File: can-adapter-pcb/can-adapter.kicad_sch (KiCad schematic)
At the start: 0 parts

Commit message: can-adapter-pcb: Add PIC18 microcontroller to schematic with ICSP programming header
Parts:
- added IC1: PIC18F26Q83T-I_5N, QFN65P600X600X100-29N-D, symbol PIC18F26Q83T-I5N:PIC18F26Q83T-I_5N
- added J1: ICSP, symbol Connector:Conn_01x06_Socket
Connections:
- new net +5V: IC1.17 (VDD), J1.2 (Pin_2)
- new net GND: IC1.16 (VSS_2), IC1.29 (EP), IC1.5 (VSS_1), J1.3 (Pin_3)
- new net ICSPCLK: IC1.25 (RB7/ICSPDAT), J1.5 (Pin_5)
- new net ICSPDAT: IC1.24 (RB6/ICSPCLK), J1.4 (Pin_4)
- new net VPP: IC1.26 (RE3/~{MCLR}/VPP), J1.1 (Pin_1)
- no-connect marks 0 -> 1

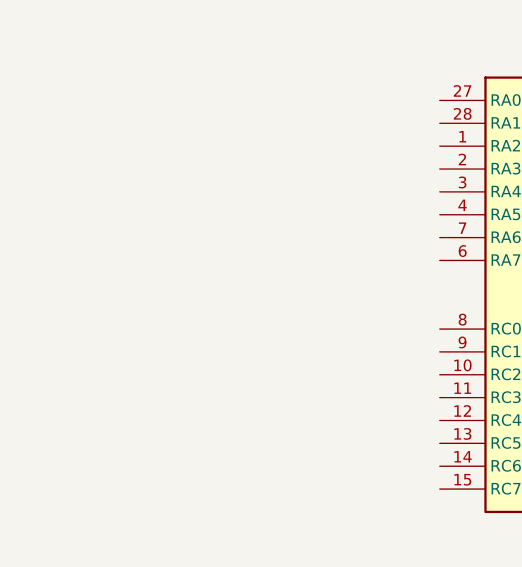
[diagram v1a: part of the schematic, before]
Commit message: can-adapter-pcb: Add tank and decoupling capacitor
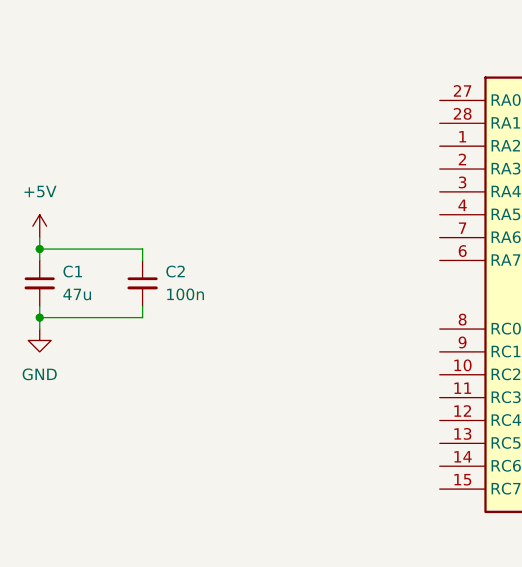
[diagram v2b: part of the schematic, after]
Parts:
- added C1: 47u, symbol Device:C_Small
- added C2: 100n, symbol Device:C_Small
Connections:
- net +5V: now also C1.1, C2.1
- net GND: now also C1.2, C2.2

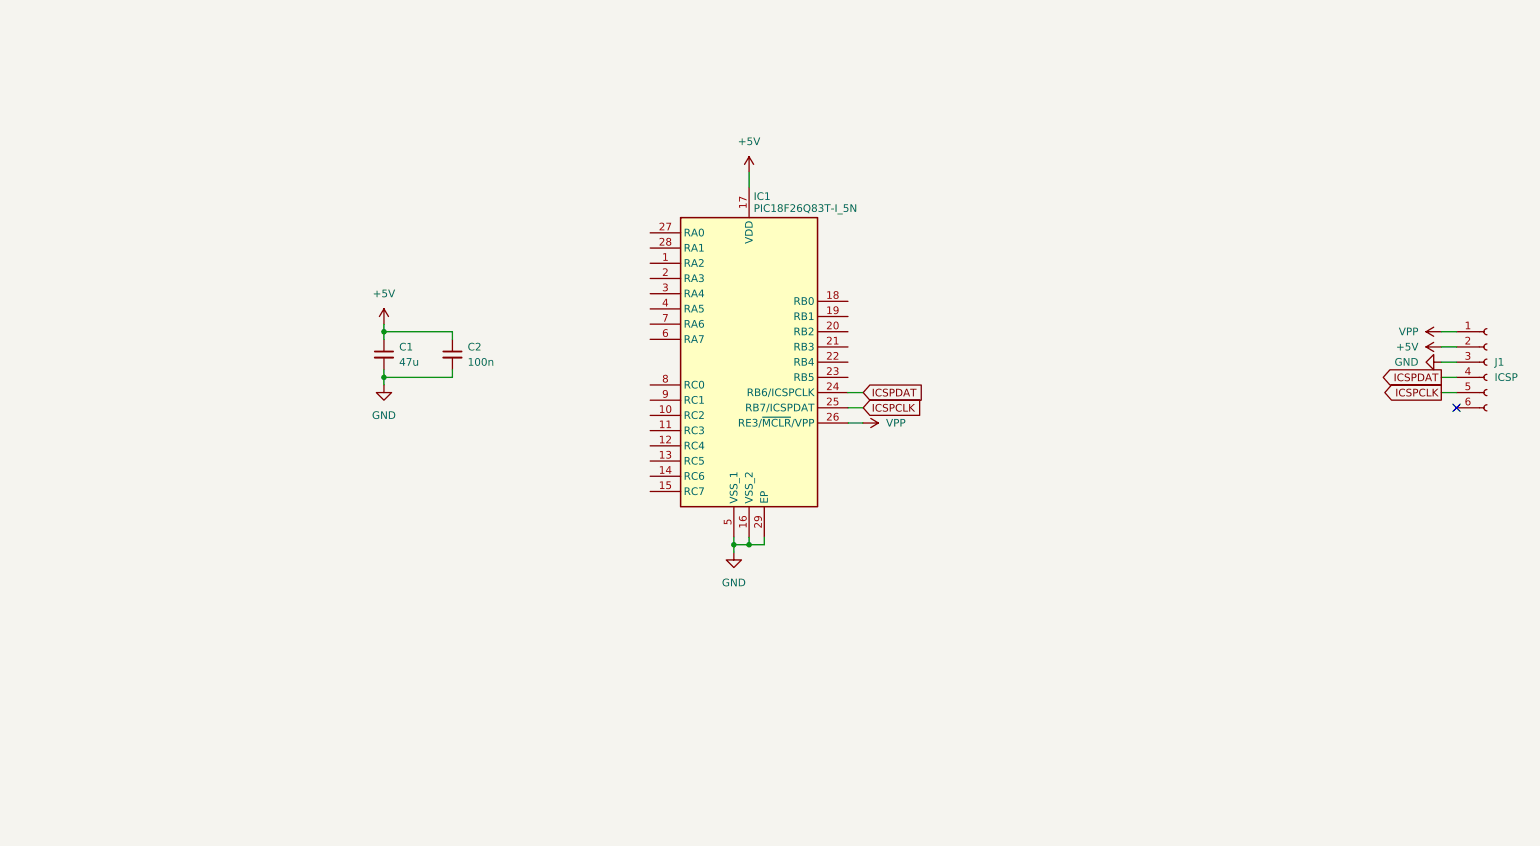
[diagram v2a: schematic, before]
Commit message: can-adapter-pcb: Add CAN transceiver to schematic
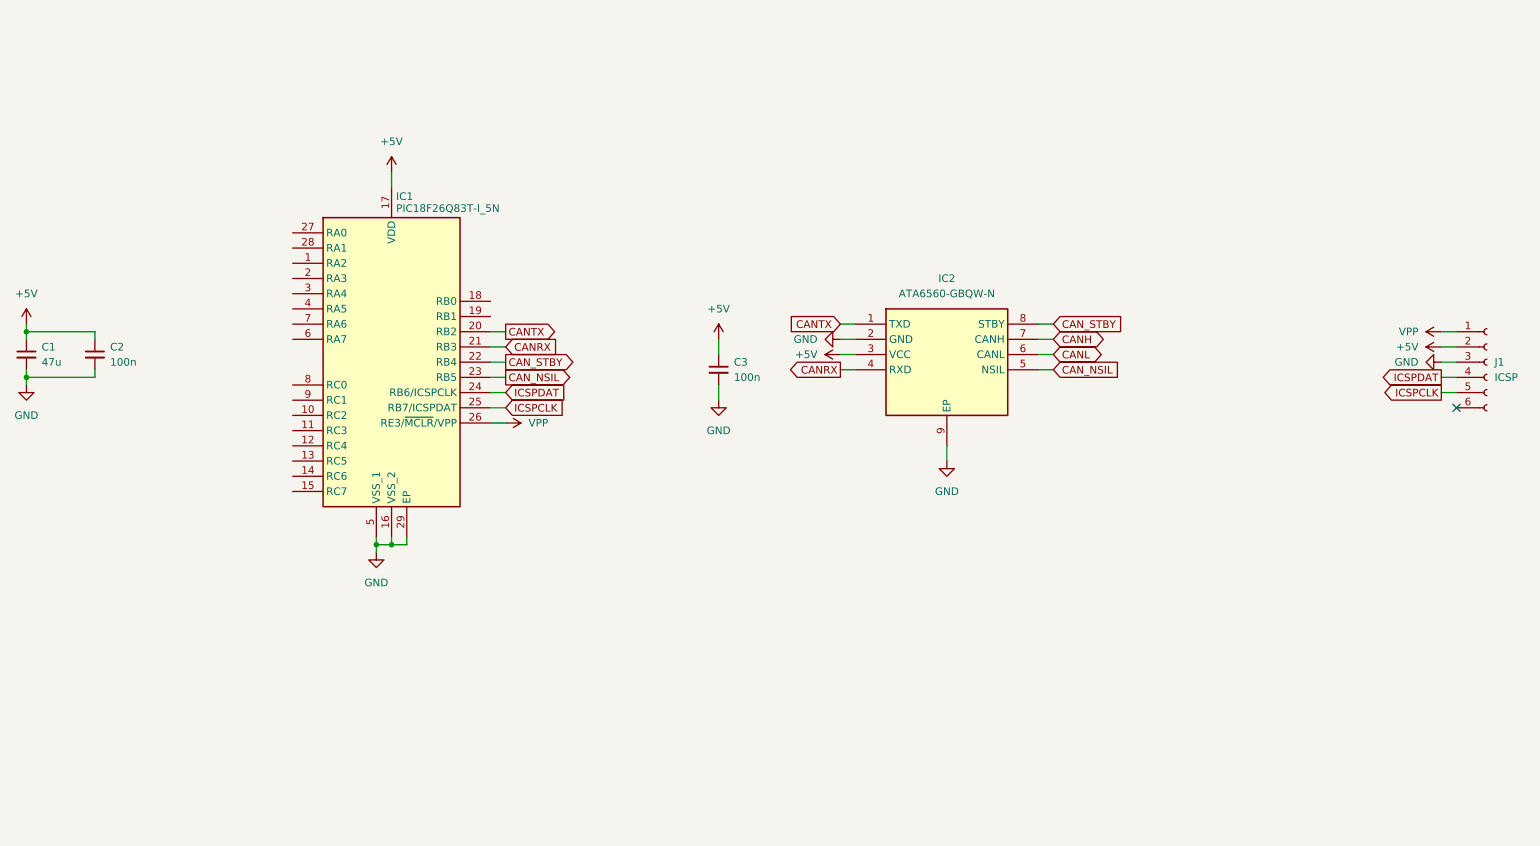
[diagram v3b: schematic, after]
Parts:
- added C3: 100n, symbol Device:C_Small
- added IC2: ATA6560-GBQW-N, SON65P300X300X90-9N-D, symbol ATA6560-GBQW-N:ATA6560-GBQW-N
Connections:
- net +5V: now also C3.1, IC2.3 (VCC)
- net GND: now also C3.2, IC2.2 (GND), IC2.9 (EP)
- net CANTX: now reaches IC1.20 (RB2)
- net CANTX: now also IC2.1 (TXD)
- net CANRX: now reaches IC1.21 (RB3)
- net CANRX: now also IC2.4 (RXD)
- net CAN_STBY: now reaches IC1.22 (RB4)
- net CAN_STBY: now also IC2.8 (STBY)
- net CAN_NSIL: now reaches IC1.23 (RB5)
- net CAN_NSIL: now also IC2.5 (NSIL)
- new net CANH: IC2.7 (CANH)
- new net CANL: IC2.6 (CANL)
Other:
- moved on the sheet: C1, C2, IC1

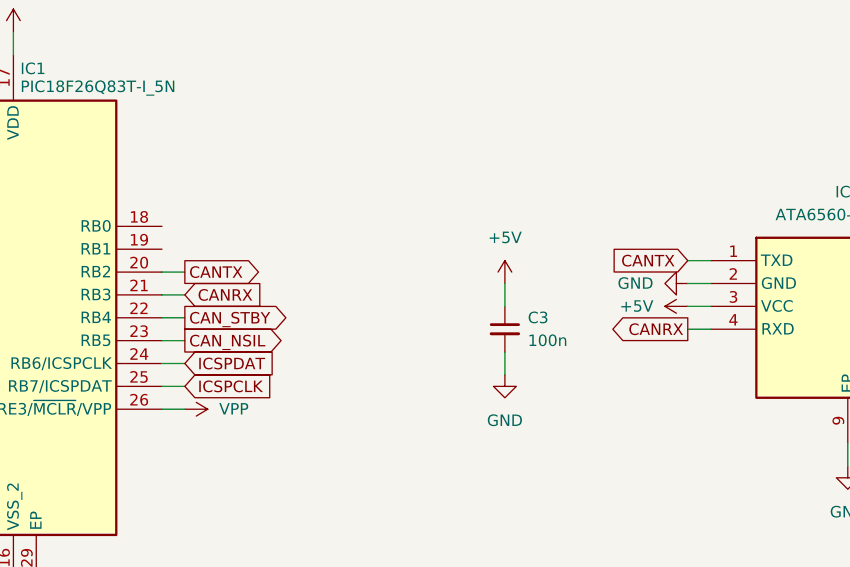
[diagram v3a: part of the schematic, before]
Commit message: can-adapter-pcb: Swap pins around, add UART debug pins on MCU
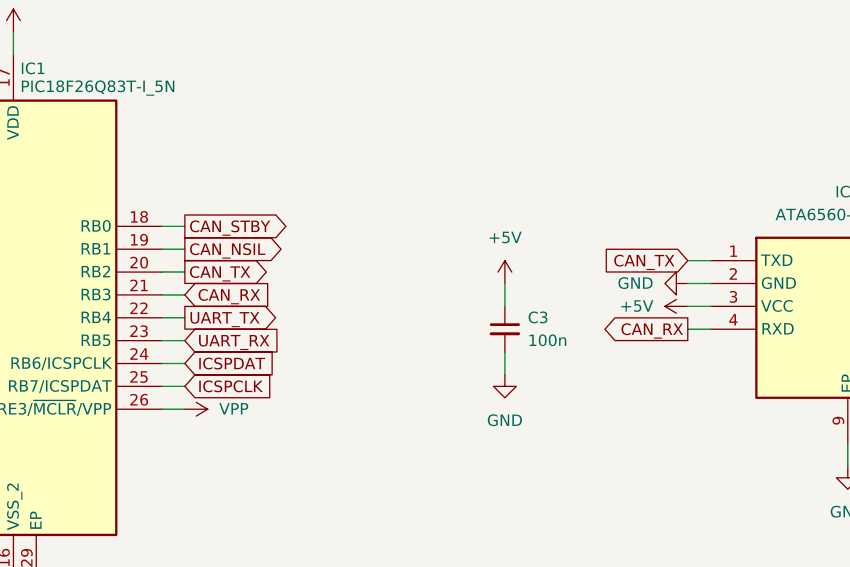
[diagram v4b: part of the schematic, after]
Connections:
- net CAN_NSIL: now also IC1.19 (RB1); no longer IC1.23 (RB5)
- net CAN_STBY: now also IC1.18 (RB0); no longer IC1.22 (RB4)
- net CANRX renamed CAN_RX
- net CANTX renamed CAN_TX
- new net UART_RX: IC1.23 (RB5)
- new net UART_TX: IC1.22 (RB4)
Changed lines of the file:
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@@
+	(wire
+		(pts
+			(xy 100.33 88.9) (xy 102.87 88.9)
+		)
+		(stroke
+			(width 0)
+			(type default)
+		)
+	)
 	(wire
 		(pts
@@
 	(wire
 		(pts
+			(xy 100.33 86.36) (xy 102.87 86.36)
+		)
+		(stroke
+			(width 0)
+			(type default)
+		)
+	)
+	(wire
+		(pts
 			(xy 100.33 101.6) (xy 102.87 101.6)
 		)
@@
 	)
 	(global_label "CAN_STBY"
+		(shape output)
+		(at 102.87 86.36 0)
+		(fields_autoplaced yes)
+		(effects
+			(font
+				(size 1.27 1.27)
+			)
+			(justify left)
+		)
+		(property "Intersheetrefs" "${INTERSHEET_REFS}"
+			(at 115.0476 86.36 0)
+			(effects
+				(font
+					(size 1.27 1.27)
+				)
+				(justify left)
+				(hide yes)
+			)
+		)
+	)
+	(global_label "CAN_STBY"
 		(shape input)
 		(at 194.31 90.17 0)
@@
 		(property "Intersheetrefs" "${INTERSHEET_REFS}"
 			(at 113.7776 104.14 0)
+			(effects
+				(font
+					(size 1.27 1.27)
+				)
+				(justify left)
+				(hide yes)
+			)
+		)
+	)
+	(global_label "CAN_NSIL"
+		(shape output)
+		(at 102.87 88.9 0)
+		(fields_autoplaced yes)
+		(effects
+			(font
+				(size 1.27 1.27)
+			)
+			(justify left)
+		)
+		(property "Intersheetrefs" "${INTERSHEET_REFS}"
+			(at 114.6848 88.9 0)
 			(effects
 				(font
@@
 		)
 	)
-	(global_label "CANRX"
+	(global_label "CAN_RX"
 		(shape output)
 		(at 158.75 97.79 180)
@@
 		)
 		(property "Intersheetrefs" "${INTERSHEET_REFS}"
-			(at 149.5962 97.79 0)
+			(at 148.6286 97.79 0)
 			(effects
 				(font
@@
 		)
 	)
-	(global_label "CANTX"
+	(global_label "CAN_TX"
 		(shape output)
 		(at 102.87 91.44 0)
@@
 		)
 		(property "Intersheetrefs" "${INTERSHEET_REFS}"
-			(at 111.7214 91.44 0)
+			(at 112.689 91.44 0)
 			(effects
 				(font
@@
 		)
 	)
+	(global_label "CAN_RX"
+		(shape input)
+		(at 102.87 93.98 0)
+		(fields_autoplaced yes)
+		(effects
+			(font
+				(size 1.27 1.27)
+			)
+			(justify left)
+		)
+		(property "Intersheetrefs" "${INTERSHEET_REFS}"
+			(at 112.9914 93.98 0)
+			(effects
+				(font
+					(size 1.27 1.27)
+				)
+				(justify left)
+				(hide yes)
+			)
+		)
+	)
+	(global_label "CAN_TX"
+		(shape input)
+		(at 158.75 90.17 180)
+		(fields_autoplaced yes)
+		(effects
+			(font
+				(size 1.27 1.27)
+			)
+			(justify right)
+		)
+		(property "Intersheetrefs" "${INTERSHEET_REFS}"
+			(at 148.931 90.17 0)
+			(effects
+				(font
+					(size 1.27 1.27)
+				)
+				(justify right)
+				(hide yes)
+			)
+		)
+	)
 	(global_label "CAN_NSIL"
-		(shape output)
+		(shape input)
+		(at 194.31 97.79 0)
+		(fields_autoplaced yes)
+		(effects
+			(font
+				(size 1.27 1.27)
+			)
+			(justify left)
+		)
+		(property "Intersheetrefs" "${INTERSHEET_REFS}"
+			(at 206.1248 97.79 0)
+			(effects
+				(font
+					(size 1.27 1.27)
+				)
+				(justify left)
+				(hide yes)
+			)
+		)
+	)
+	(global_label "UART_TX"
+		(shape output)
+		(at 102.87 96.52 0)
+		(fields_autoplaced yes)
+		(effects
+			(font
+				(size 1.27 1.27)
+			)
+			(justify left)
+		)
+		(property "Intersheetrefs" "${INTERSHEET_REFS}"
+			(at 113.6566 96.52 0)
+			(effects
+				(font
+					(size 1.27 1.27)
+				)
+				(justify left)
+				(hide yes)
+			)
+		)
+	)
+	(global_label "UART_RX"
+		(shape input)
 		(at 102.87 99.06 0)
 		(fields_autoplaced yes)
@@
 		)
 		(property "Intersheetrefs" "${INTERSHEET_REFS}"
-			(at 114.6848 99.06 0)
-			(effects
-				(font
-					(size 1.27 1.27)
-				)
-				(justify left)
-				(hide yes)
-			)
-		)
-	)
-	(global_label "CANRX"
-		(shape input)
-		(at 102.87 93.98 0)
-		(fields_autoplaced yes)
-		(effects
-			(font
-				(size 1.27 1.27)
-			)
-			(justify left)
-		)
-		(property "Intersheetrefs" "${INTERSHEET_REFS}"
-			(at 112.0238 93.98 0)
-			(effects
-				(font
-					(size 1.27 1.27)
-				)
-				(justify left)
-				(hide yes)
-			)
-		)
-	)
-	(global_label "CANTX"
-		(shape input)
-		(at 158.75 90.17 180)
-		(fields_autoplaced yes)
-		(effects
-			(font
-				(size 1.27 1.27)
-			)
-			(justify right)
-		)
-		(property "Intersheetrefs" "${INTERSHEET_REFS}"
-			(at 149.8986 90.17 0)
-			(effects
-				(font
-					(size 1.27 1.27)
-				)
-				(justify right)
-				(hide yes)
-			)
-		)
-	)
-	(global_label "CAN_NSIL"
-		(shape input)
-		(at 194.31 97.79 0)
-		(fields_autoplaced yes)
-		(effects
-			(font
-				(size 1.27 1.27)
-			)
-			(justify left)
-		)
-		(property "Intersheetrefs" "${INTERSHEET_REFS}"
-			(at 206.1248 97.79 0)
-			(effects
-				(font
-					(size 1.27 1.27)
-				)
-				(justify left)
-				(hide yes)
-			)
-		)
-	)
-	(global_label "CAN_STBY"
-		(shape output)
-		(at 102.87 96.52 0)
-		(fields_autoplaced yes)
-		(effects
-			(font
-				(size 1.27 1.27)
-			)
-			(justify left)
-		)
-		(property "Intersheetrefs" "${INTERSHEET_REFS}"
-			(at 115.0476 96.52 0)
-			(effects
-				(font
+			(at 113.959 99.06 0)
+			(effects
+				(font

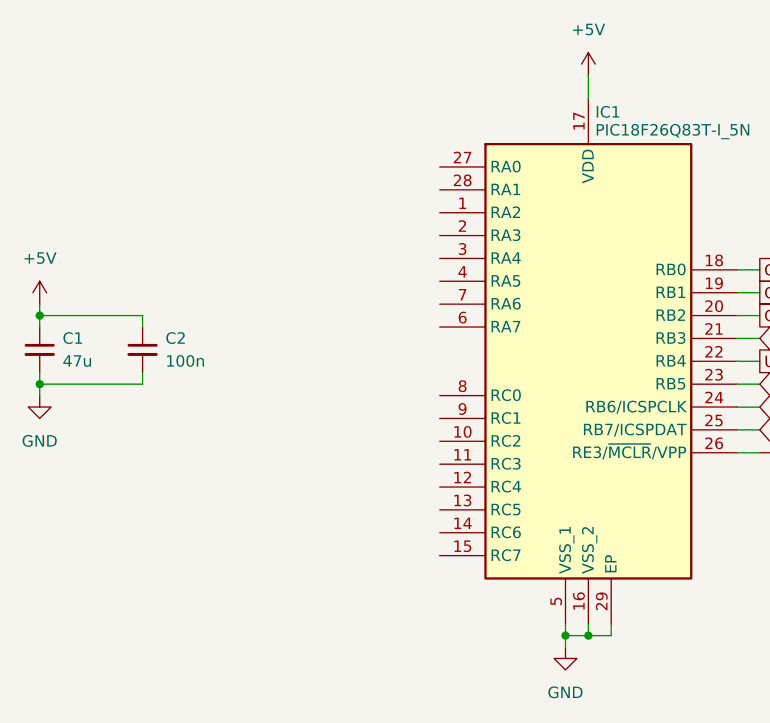
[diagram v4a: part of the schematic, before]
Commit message: can-adapter-pcb: Add connectors for other MCU pins
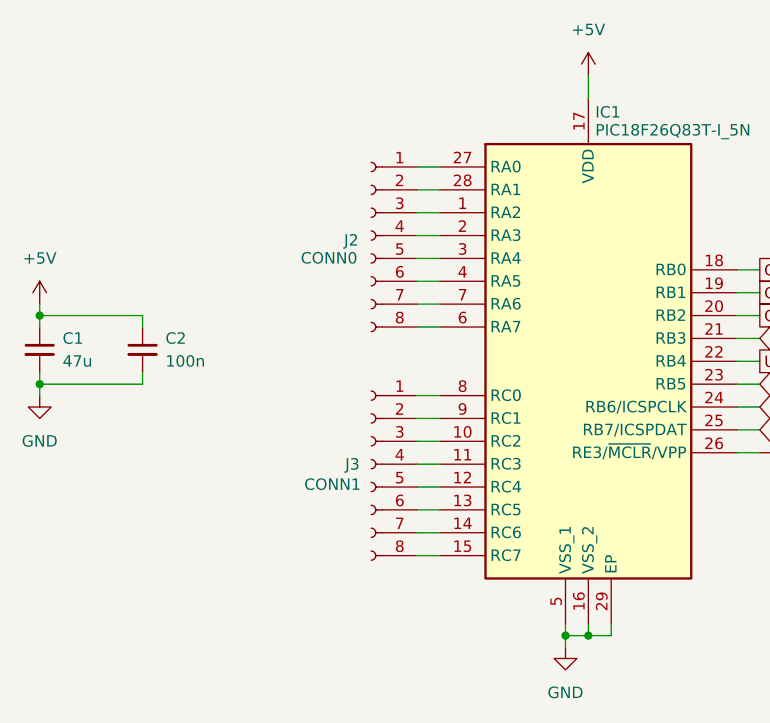
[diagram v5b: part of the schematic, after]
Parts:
- added J2: CONN0, symbol Connector:Conn_01x08_Socket
- added J3: CONN1, symbol Connector:Conn_01x08_Socket
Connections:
- net at IC1.1 (RA2): now also J2.3 (Pin_3)
- net at IC1.10 (RC2): now also J3.3 (Pin_3)
- net at IC1.11 (RC3): now also J3.4 (Pin_4)
- net at IC1.12 (RC4): now also J3.5 (Pin_5)
- net at IC1.13 (RC5): now also J3.6 (Pin_6)
- net at IC1.14 (RC6): now also J3.7 (Pin_7)
- net at IC1.15 (RC7): now also J3.8 (Pin_8)
- net at IC1.2 (RA3): now also J2.4 (Pin_4)
- net at IC1.27 (RA0): now also J2.1 (Pin_1)
- net at IC1.28 (RA1): now also J2.2 (Pin_2)
- net at IC1.3 (RA4): now also J2.5 (Pin_5)
- net at IC1.4 (RA5): now also J2.6 (Pin_6)
- net at IC1.6 (RA7): now also J2.8 (Pin_8)
- net at IC1.7 (RA6): now also J2.7 (Pin_7)
- net at IC1.8 (RC0): now also J3.1 (Pin_1)
- net at IC1.9 (RC1): now also J3.2 (Pin_2)
